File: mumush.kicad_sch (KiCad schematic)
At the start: 40 parts

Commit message: clean
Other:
- note added: "Light"
- note added: "Power"
- note added: "Screen"
- note removed: "LIGHT"
- note removed: "SCREEN"
- moved on the sheet: C?, F?, FL?, J?, PS?, RV?, U?

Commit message: disable ACDC converter.
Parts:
- added J?: Conn_01x02, symbol Connector_Generic:Conn_01x02
- gave numbers to parts that had none: 40
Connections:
- net +12V: now also J?.1 (Pin_1)
- net GND: now also J?.2 (Pin_2)
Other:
- note added: "Optional, remove # to activate."
- moved on the sheet: U6

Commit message: progress on schematic.
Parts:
- removed #C1: 0.1uF/275V, symbol Device:C
- removed #C3: 220uF, symbol Device:C_Polarized
- removed #F1: Fuse, symbol Device:Fuse
- removed #FL1: Filter_EMI_LL_1423, symbol Device:Filter_EMI_LL_1423
- removed #J1, J2, J3, J4, J6, J7: Screw_Terminal_01x02, symbol Connector:Screw_Terminal_01x02
- removed #PS1: HLK-10M12, myFootprints:Converter_ACDC_HiLink_HLK-10Mxx, symbol mySymbols:HLK-10M12
- removed #RV1: Varistor, symbol Device:Varistor
- removed J?: Conn_01x02, symbol Connector_Generic:Conn_01x02
- removed JP1, JP2: Jumper_3_Open, symbol Jumper:Jumper_3_Open
- removed U13, U7: IRLML6344, myFootprints:SOT-23, symbol mySymbols:IRLML6344
- added D1, D2, D3, D4, D5: LED, LED_SMD:LED_0603_1608Metric_Pad1.05x0.95mm_HandSolder, symbol Device:LED
- added J1: Screw_Terminal_01x02, TerminalBlock:TerminalBlock_bornier-2_P5.08mm, symbol Connector:Screw_Terminal_01x02
- added J2, J3: Conn_01x02, Connector_PinHeader_2.54mm:PinHeader_1x02_P2.54mm_Horizontal, symbol Connector_Generic:Conn_01x02
- added J4, J6, J7: Conn_01x02, symbol Connector_Generic:Conn_01x02
- added R10, R11, R12, R9: 390, Resistor_SMD:R_0603_1608Metric_Pad0.98x0.95mm_HandSolder, symbol Device:R
- added R13: 1k, Resistor_SMD:R_0603_1608Metric_Pad0.98x0.95mm_HandSolder, symbol Device:R
- added SW1, SW2: SW_SPDT, Button_Switch_THT:SW_CuK_OS102011MA1QN1_SPDT_Angled, symbol Switch:SW_SPDT
- added SW3, SW4, SW5: SW_Push, Button_Switch_THT:SW_PUSH_6mm_H5mm, symbol Switch:SW_Push
- C2: value C_Small -> 100nF; footprint (none) -> Capacitor_SMD:C_0603_1608Metric_Pad1.08x0.95mm_HandSolder
- R1, R2, R3, R4, R5, R6, R7, R8: footprint (none) -> Resistor_SMD:R_0603_1608Metric_Pad0.98x0.95mm_HandSolder
- TH1: footprint (none) -> Connector_JST:JST_XH_B2B-XH-A_1x02_P2.50mm_Vertical
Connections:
- net +12V: now also J1.1 (Pin_1), J2.2 (Pin_2), J3.1 (Pin_1), R13.2
- net FAN: now also U8.1 (G), R9.2
- net GND: now also D1.1 (K), D2.1 (K), D3.1 (K), D4.1 (K), D5.1 (K), J1.2 (Pin_2), SW3.2, SW4.2, SW5.2
- net HEAT: now also R11.2
- net HUMIDIFIER: now also U14.1 (G), R10.2
- net LIGHT: now also R12.2
- net at U8.3 (D): now also SW1.2 (B)
- net at U10.3 (D): now also J3.2 (Pin_2)
- net at J5.4 (GND): now also SW2.1 (A); no longer U14.3 (D)
- new net: J4.1 (Pin_1), U9. (4)
- new net: J4.2 (Pin_2), U9. (4)
- new net: D2.2 (A), R10.1
- new net: J6.1 (Pin_1), U12. (4)
- new net: J6.2 (Pin_2), U12. (4)
- new net: D1.2 (A), R9.1
- new net: SW2.3 (C), U15. (4)
- new net: J7.1 (Pin_1), U15. (4)
- new net: J7.2 (Pin_2), U15. (4)
- new net: D4.2 (A), R12.1
- new net: SW1.3 (C), U9. (4)
- new net: D5.2 (A), R13.1
- new net: J2.1 (Pin_1), SW1.1 (A)
- new net: D3.2 (A), R11.1
- new net: SW2.2 (B), U14.3 (D)
- new net BTN1: SW3.1
- new net BTN2: SW4.1
- new net BTN3: SW5.1
- no-connect marks 0 -> 3
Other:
- note added: "Indicator leds"
- note added: "User control"
- note removed: "Optional, remove # to activate."
- moved on the sheet: C2, J5, R1, R2, R3, R4, R5, R6, R7, R8, TH1, U1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

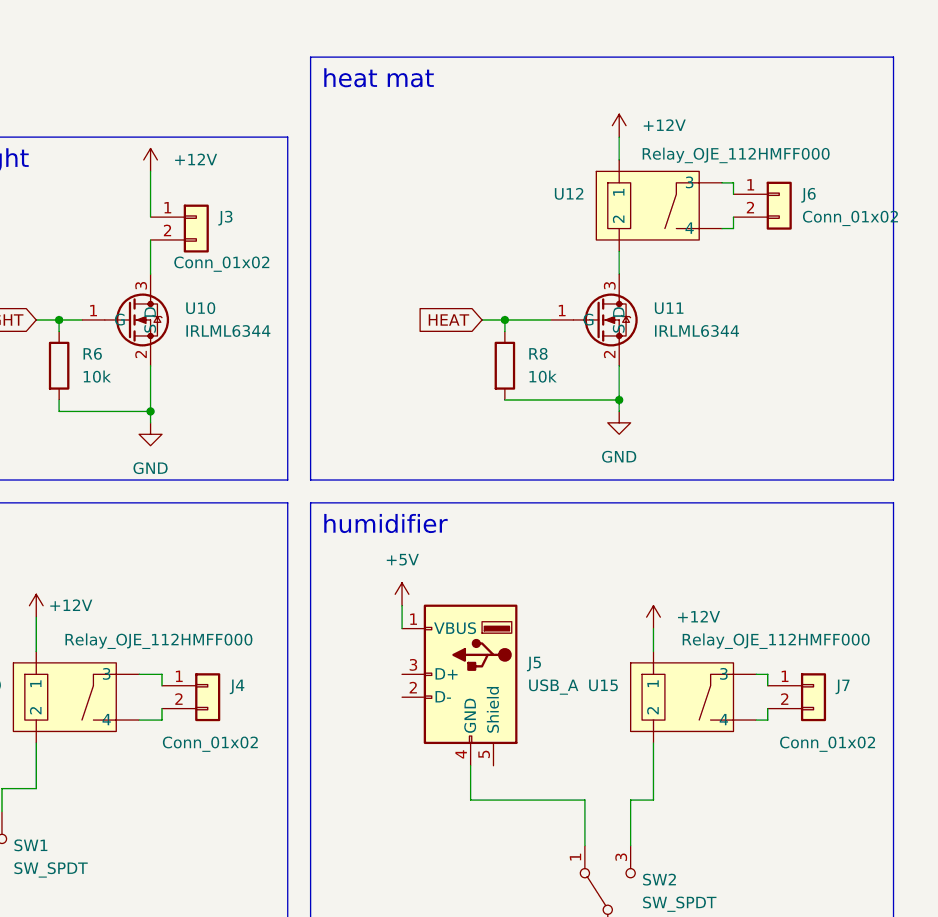
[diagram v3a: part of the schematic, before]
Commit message: choose better footprints.
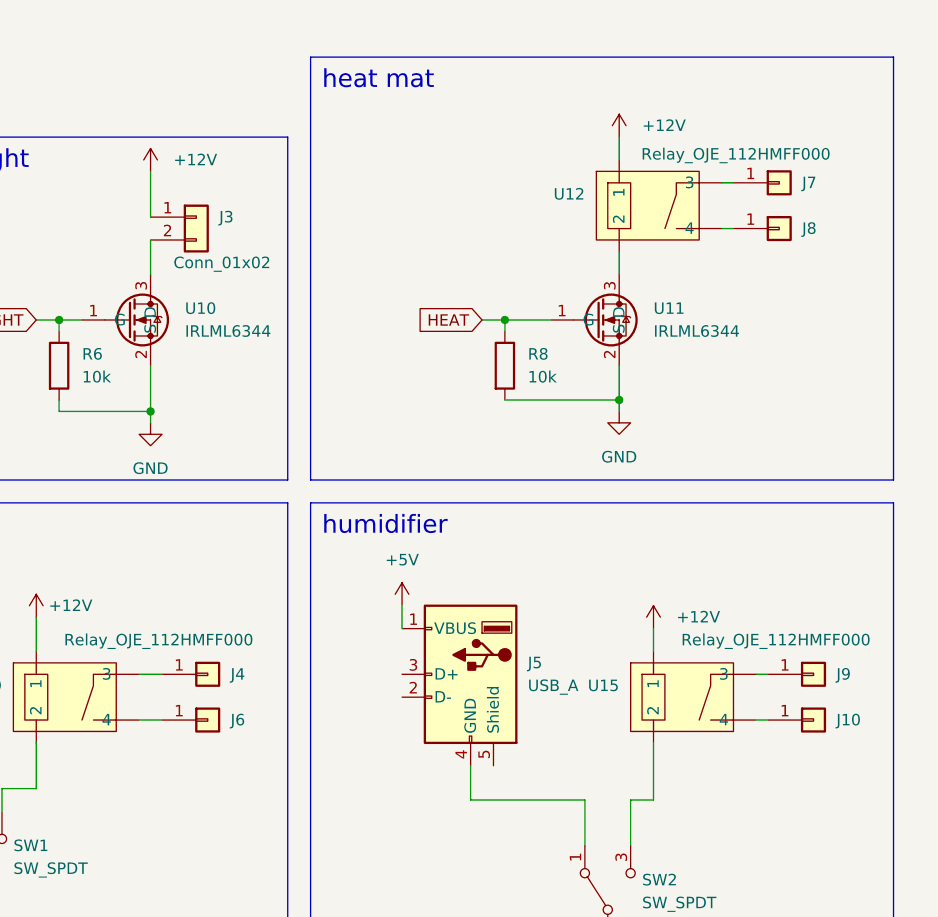
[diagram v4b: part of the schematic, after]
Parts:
- removed J4, J6, J7: Conn_01x02, symbol Connector_Generic:Conn_01x02
- added J10, J4, J6, J7, J8, J9: Conn_01x01, myFootprints:cosse, symbol Connector_Generic:Conn_01x01
- J5: footprint (none) -> Connector_USB:USB_A_CONNFLY_DS1095-WNR0
- SW1, SW2: footprint Button_Switch_THT:SW_CuK_OS102011MA1QN1_SPDT_Angled -> myFootprints:switch SPDT
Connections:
- new net: J6.1 (Pin_1), U9. (4)
- new net: J8.1 (Pin_1), U12. (4)
- new net: J9.1 (Pin_1), U15. (4)
- new net: J4.1 (Pin_1), U9. (4)
- new net: J10.1 (Pin_1), U15. (4)
- new net: J7.1 (Pin_1), U12. (4)

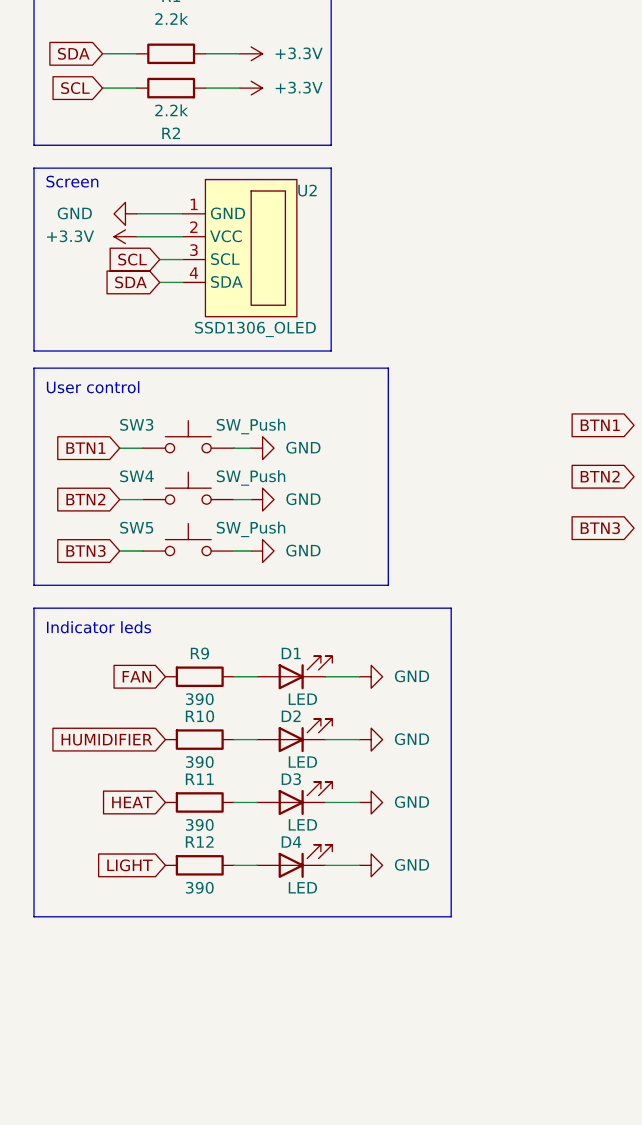
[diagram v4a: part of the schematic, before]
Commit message: update OLED screen.
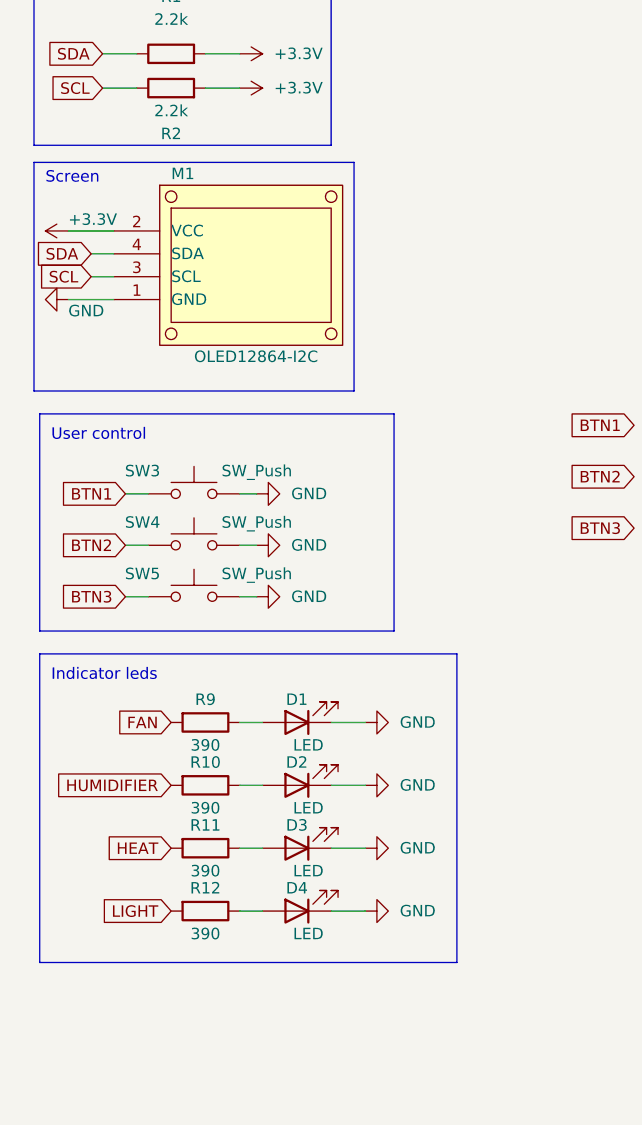
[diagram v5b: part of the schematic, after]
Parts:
- removed U2: SSD1306_OLED, symbol mySymbols:SSD1306_OLED
- added M1: OLED12864-I2C, myFootprints:OLED12864-I2C_TH_6mm, symbol mySymbols:OLED12864-I2C
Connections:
- net +3.3V: now also M1.2 (VCC)
- net GND: now also M1.1 (GND)
- net SCL: now also M1.3 (SCL)
- net SDA: now also M1.4 (SDA)
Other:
- moved on the sheet: D1, D2, D3, D4, R10, R11, R12, R9, SW3, SW4, SW5

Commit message: Update
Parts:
- J2: value Conn_01x02 -> header_fan
- J3: value Conn_01x02 -> header_light
- U12: value Relay_OJE_112HMFF000 -> Relay_heat
- U15: value Relay_OJE_112HMFF000 -> Relay_humidifier
- U9: value Relay_OJE_112HMFF000 -> Relay_fan
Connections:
- net +12V: now also U12.1, U15.1, U9.1; no longer U12. (4), U15. (4), U9. (4)
- net at J6.1 (Pin_1): now also U9.4; no longer U9. (4)
- net at J8.1 (Pin_1): now also U12.4; no longer U12. (4)
- net at J9.1 (Pin_1): now also U15.3; no longer U15. (4)
- net at J4.1 (Pin_1): now also U9.3; no longer U9. (4)
- net at J10.1 (Pin_1): now also U15.4; no longer U15. (4)
- net at SW2.3 (C): now also U15.2; no longer U15. (4)
- net at U11.3 (D): now also U12.2; no longer U12. (4)
- net at SW1.3 (C): now also U9.2; no longer U9. (4)
- net at J7.1 (Pin_1): now also U12.3; no longer U12. (4)
- no-connect marks 3 -> 31
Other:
- moved on the sheet: C2, D1, D2, D3, D4, D5, J1, J10, J2, J3, J4, J5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

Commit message: PCB progress.
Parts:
- TH1: footprint Connector_JST:JST_XH_B2B-XH-A_1x02_P2.50mm_Vertical -> Connector_PinHeader_2.54mm:PinHeader_1x02_P2.54mm_Horizontal
- U1: footprint Sensor:Aosong_DHT11_5.5x12.0_P2.54mm -> Connector_PinHeader_2.54mm:PinHeader_1x04_P2.54mm_Horizontal
- U5: footprint Connector_PinHeader_2.54mm:PinHeader_1x08_P2.54mm_Vertical -> Connector_PinHeader_2.54mm:PinHeader_1x08_P2.54mm_Horizontal
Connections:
- net +12V: now also J2.1 (Pin_1); no longer J2.2 (Pin_2)
- net BTN1: now also U4.26 (D14)
- net BTN2: now also U4.27 (D12)
- net BTN3: now also U4.28 (D13)
- net DHT: now also U4.7 (TX2)
- net FAN: now also U4.10 (D19)
- net HEAT: now also U4.19 (D34)
- net HUMIDIFIER: now also U4.8 (D5)
- net LIGHT: now also U4.9 (D18)
- net SCL: now also U4.14 (D22)
- net SDA: now also U4.11 (D21)
- net at SW1.1 (A): now also J2.2 (Pin_2); no longer J2.1 (Pin_1)
- no-connect marks 31 -> 21
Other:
- moved on the sheet: J2

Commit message: V1
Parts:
- removed J5: USB_A, Connector_USB:USB_A_CONNFLY_DS1095-WNR0, symbol Connector:USB_A
- added J5: humidifier, Connector_PinHeader_2.54mm:PinHeader_1x02_P2.54mm_Horizontal, symbol Connector_Generic:Conn_01x02
- TH1: footprint Connector_PinHeader_2.54mm:PinHeader_1x02_P2.54mm_Horizontal -> Connector_PinHeader_2.54mm:PinHeader_1x02_P2.54mm_Vertical
- U1: footprint Connector_PinHeader_2.54mm:PinHeader_1x04_P2.54mm_Horizontal -> Connector_PinHeader_2.54mm:PinHeader_1x04_P2.54mm_Vertical
- U5: footprint Connector_PinHeader_2.54mm:PinHeader_1x08_P2.54mm_Horizontal -> Connector_PinHeader_2.54mm:PinHeader_1x08_P2.54mm_Vertical
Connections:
- net +12V: now also J5.1 (Pin_1)
- net at SW2.1 (A): now also J5.2 (Pin_2)
- no-connect marks 21 -> 18
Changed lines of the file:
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@@
   (no_connect (at 120.015 111.76))
   (no_connect (at 132.08 34.29))
-  (no_connect (at 229.87 108.585))
   (no_connect (at 120.015 124.46))
   (no_connect (at 132.08 31.75))
   (no_connect (at 120.015 91.44))
   (no_connect (at 89.535 106.68))
-  (no_connect (at 240.03 118.745))
   (no_connect (at 120.015 99.06))
-  (no_connect (at 229.87 111.125))
   (no_connect (at 120.015 93.98))
   (no_connect (at 89.535 91.44))
@@
     (stroke (width 0) (type default) (color 0 0 0 0))
   )
-  (wire (pts (xy 229.87 100.965) (xy 229.87 103.505))
-    (stroke (width 0) (type default) (color 0 0 0 0))
-  )
   (wire (pts (xy 265.43 59.055) (xy 266.7 59.055))
     (stroke (width 0) (type default) (color 0 0 0 0))
@@
     (stroke (width 0) (type default) (color 0 0 0 0))
   )
+  (wire (pts (xy 237.49 102.235) (xy 237.49 109.855))
+    (stroke (width 0) (type default) (color 0 0 0 0))
+  )
   (wire (pts (xy 34.29 69.85) (xy 38.1 69.85))
     (stroke (width 0) (type default) (color 0 0 0 0))
@@
     (stroke (width 0) (type default) (color 0 0 0 0))
   )
-  (wire (pts (xy 237.49 118.745) (xy 237.49 122.555))
+  (wire (pts (xy 237.49 112.395) (xy 237.49 122.555))
     (stroke (width 0) (type default) (color 0 0 0 0))
   )
@@
     (pin "2")
   )
+  (symbol (lib_id "power:+12V") (at 237.49 102.235 0) (unit 1)
+    (in_bom yes) (on_board yes) (fields_autoplaced)
+    (property "Reference" "#PWR0101" (id 0) (at 237.49 106.045 0)
+      (effects (font (size 1.27 1.27)) hide)
+    )
+    (property "Value" "+12V" (id 1) (at 240.03 100.9649 0)
+      (effects (font (size 1.27 1.27)) (justify left))
+    )
+    (property "Footprint" "" (id 2) (at 237.49 102.235 0)
+      (effects (font (size 1.27 1.27)) hide)
+    )
+    (property "Datasheet" "" (id 3) (at 237.49 102.235 0)
+      (effects (font (size 1.27 1.27)) hide)
+    )
+    (pin "1")
+  )
   (symbol (lib_id "power:GND") (at 19.05 93.345 270) (unit 1)
     (in_bom yes) (on_board yes)
@@
       (effects (font (size 1.27 1.27)) (justify left))
     )
-    (property "Footprint" "Connector_PinHeader_2.54mm:PinHeader_1x08_P2.54mm_Horizontal" (id 2) (at 139.7 44.45 0)
+    (property "Footprint" "Connector_PinHeader_2.54mm:PinHeader_1x08_P2.54mm_Vertical" (id 2) (at 139.7 44.45 0)
       (effects (font (size 1.27 1.27)) hide)
     )
@@
     (pin "1")
   )
-  (symbol (lib_id "Connector:USB_A") (at 237.49 108.585 0) (mirror y) (unit 1)
-    (in_bom yes) (on_board yes) (fields_autoplaced)
-    (property "Reference" "J5" (id 0) (at 243.84 107.3149 0)
-      (effects (font (size 1.27 1.27)) (justify right))
-    )
-    (property "Value" "USB_A" (id 1) (at 243.84 109.8549 0)
-      (effects (font (size 1.27 1.27)) (justify right))
-    )
-    (property "Footprint" "Connector_USB:USB_A_CONNFLY_DS1095-WNR0" (id 2) (at 233.68 109.855 0)
-      (effects (font (size 1.27 1.27)) hide)
-    )
-    (property "Datasheet" " ~" (id 3) (at 233.68 109.855 0)
-      (effects (font (size 1.27 1.27)) hide)
-    )
-    (pin "1")
-    (pin "2")
-    (pin "3")
-    (pin "4")
-    (pin "5")
-  )
   (symbol (lib_id "Connector_Generic:Conn_01x02") (at 171.45 109.855 0) (mirror y) (unit 1)
     (in_bom yes) (on_board yes) (fields_autoplaced)
@@
     (pin "1")
   )
-  (symbol (lib_id "power:+5V") (at 229.87 100.965 0) (unit 1)
-    (in_bom yes) (on_board yes) (fields_autoplaced)
-    (property "Reference" "#PWR037" (id 0) (at 229.87 104.775 0)
-      (effects (font (size 1.27 1.27)) hide)
-    )
-    (property "Value" "+5V" (id 1) (at 229.87 95.885 0))
-    (property "Footprint" "" (id 2) (at 229.87 100.965 0)
-      (effects (font (size 1.27 1.27)) hide)
-    )
-    (property "Datasheet" "" (id 3) (at 229.87 100.965 0)
-      (effects (font (size 1.27 1.27)) hide)
-    )
-    (pin "1")
-  )
   (symbol (lib_id "power:+12V") (at 176.53 102.235 0) (unit 1)
     (in_bom yes) (on_board yes) (fields_autoplaced)
@@
     (pin "2")
   )
+  (symbol (lib_id "Connector_Generic:Conn_01x02") (at 232.41 109.855 0) (mirror y) (unit 1)
+    (in_bom yes) (on_board yes) (fields_autoplaced)
+    (property "Reference" "J5" (id 0) (at 232.41 102.87 0))
+    (property "Value" "humidifier" (id 1) (at 232.41 105.41 0))
+    (property "Footprint" "Connector_PinHeader_2.54mm:PinHeader_1x02_P2.54mm_Horizontal" (id 2) (at 232.41 109.855 0)
+      (effects (font (size 1.27 1.27)) hide)
+    )
+    (property "Datasheet" "~" (id 3) (at 232.41 109.855 0)
+      (effects (font (size 1.27 1.27)) hide)
+    )
+    (pin "1")
+    (pin "2")
+  )
   (symbol (lib_id "power:+12V") (at 257.81 103.505 0) (unit 1)
     (in_bom yes) (on_board yes) (fields_autoplaced)
@@
       (effects (font (size 1.27 1.27)) (justify right))
     )
-    (property "Footprint" "Connector_PinHeader_2.54mm:PinHeader_1x04_P2.54mm_Horizontal" (id 2) (at 33.02 45.72 0)
+    (property "Footprint" "Connector_PinHeader_2.54mm:PinHeader_1x04_P2.54mm_Vertical" (id 2) (at 33.02 45.72 0)
       (effects (font (size 1.27 1.27)) hide)
     )
@@
       (effects (font (size 1.27 1.27)) (justify left))
     )
-    (property "Footprint" "Connector_PinHeader_2.54mm:PinHeader_1x02_P2.54mm_Horizontal" (id 2) (at 88.9 26.67 0)
+    (property "Footprint" "Connector_PinHeader_2.54mm:PinHeader_1x02_P2.54mm_Vertical" (id 2) (at 88.9 26.67 0)
       (effects (font (size 1.27 1.27)) hide)
     )
@@
       (reference "#PWR036") (unit 1) (value "GND") (footprint "")
     )
-    (path "/a12114e6-5d5e-4c72-8abf-4c6b4e2f3d45"
-      (reference "#PWR037") (unit 1) (value "+5V") (footprint "")
-    )
     (path "/2bf5f584-2194-45e2-8349-455c18ddef60"
       (reference "#PWR038") (unit 1) (value "GND") (footprint "")
@@
       (reference "#PWR041") (unit 1) (value "GND") (footprint "")
     )
+    (path "/1c65d7d8-b983-4b3e-ace7-3361aa247200"
+      (reference "#PWR0101") (unit 1) (value "+12V") (footprint "")
+    )
     (path "/ad9a1937-1531-485f-9e47-83fac7bec8a6"
       (reference "C2") (unit 1) (value "100nF") (footprint "Capacitor_SMD:C_0603_1608Metric_Pad1.08x0.95mm_HandSolder")
@@
       (reference "J4") (unit 1) (value "Conn_01x01") (footprint "myFootprints:cosse")
     )
-    (path "/861cd88f-9184-4505-a45c-1a03226283d6"
-      (reference "J5") (unit 1) (value "USB_A") (footprint "Connector_USB:USB_A_CONNFLY_DS1095-WNR0")
+    (path "/bf5a667b-c560-42dc-95ba-d1001aa5d34c"
+      (reference "J5") (unit 1) (value "humidifier") (footprint "Connector_PinHeader_2.54mm:PinHeader_1x02_P2.54mm_Horizontal")
     )
     (path "/110d7a22-54f0-4898-a9b1-66d68cc3a3e3"
@@
     )
     (path "/e83cf913-5087-4357-8217-c7899d62da75"
-      (reference "TH1") (unit 1) (value "Thermistor") (footprint "Connector_PinHeader_2.54mm:PinHeader_1x02_P2.54mm_Horizontal")
+      (reference "TH1") (unit 1) (value "Thermistor") (footprint "Connector_PinHeader_2.54mm:PinHeader_1x02_P2.54mm_Vertical")
     )
     (path "/dce3eb49-6d3f-437d-a3ba-44563216f1e4"
-      (reference "U1") (unit 1) (value "DHT11") (footprint "Connector_PinHeader_2.54mm:PinHeader_1x04_P2.54mm_Horizontal")
+      (reference "U1") (unit 1) (value "DHT11") (footprint "Connector_PinHeader_2.54mm:PinHeader_1x04_P2.54mm_Vertical")
     )
     (path "/4a739759-77eb-40c9-9a98-d99ec4ccf773"
@@
     )
     (path "/23896361-fcee-4500-b7f2-cb1b5f031f23"
-      (reference "U5") (unit 1) (value "CCS811") (footprint "Connector_PinHeader_2.54mm:PinHeader_1x08_P2.54mm_Horizontal")
+      (reference "U5") (unit 1) (value "CCS811") (footprint "Connector_PinHeader_2.54mm:PinHeader_1x08_P2.54mm_Vertical")
     )
     (path "/73dc4ed5-c99f-4a44-b8ae-b8b8e4572139"
